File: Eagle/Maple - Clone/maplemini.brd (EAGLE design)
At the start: 32 parts, among them Q1 NPN-BJT, Q2 NPN-BJT, U1 AMS1117-3.3, X1 USB-MINIB

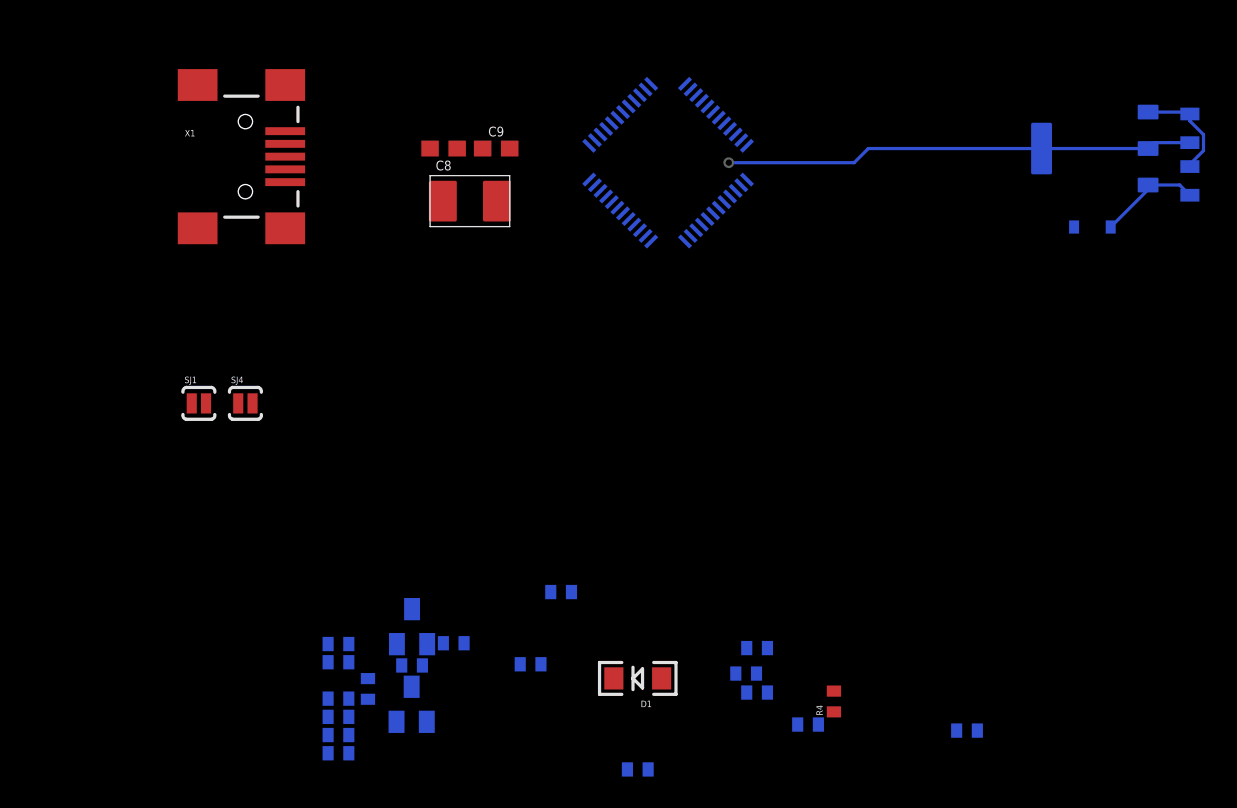
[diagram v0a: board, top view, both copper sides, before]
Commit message: reworked off proper reference boards
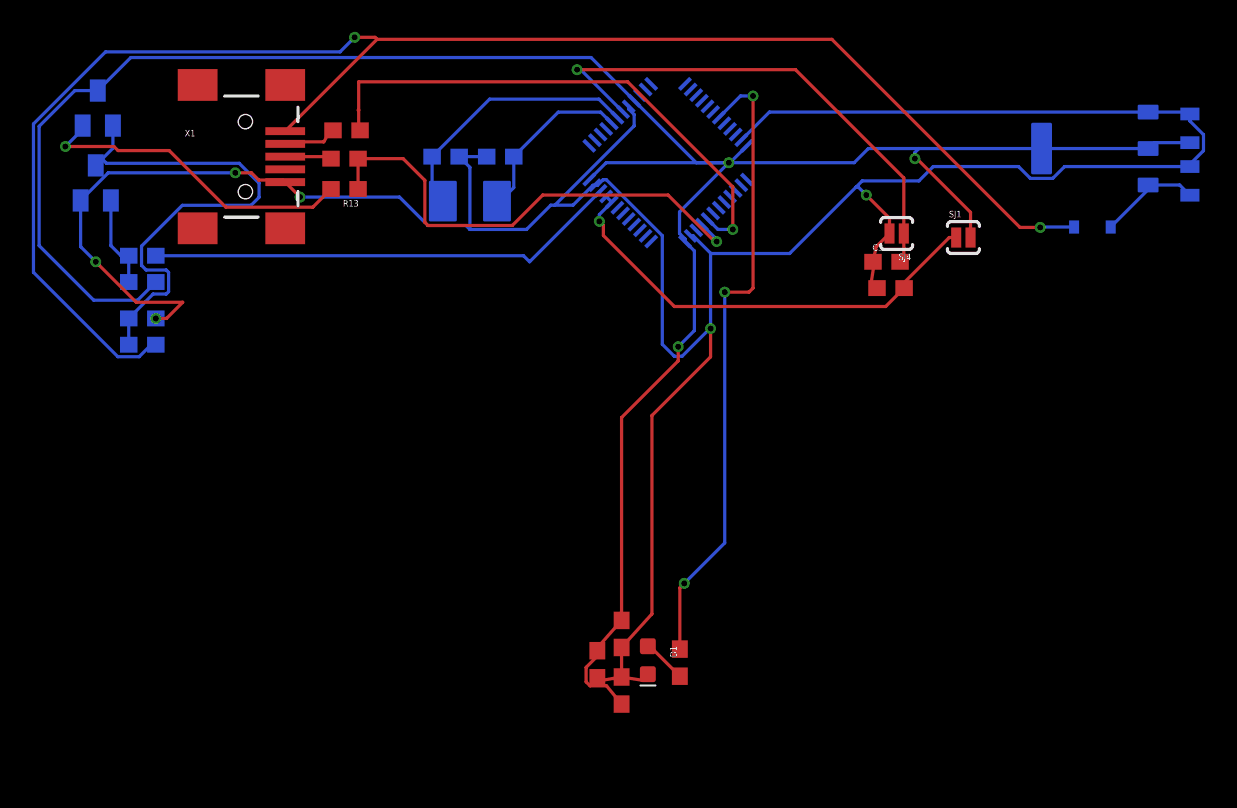
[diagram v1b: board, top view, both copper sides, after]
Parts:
- removed C10, C11: 47pF, SparkFun:C0402
- removed C4: 1uF, SparkFun:C0402
- removed Q1, Q2: NPN-BJT, SparkFun2:SOT23
- removed R10: 1.5k, SparkFun:C0402
- removed R11: 36k, SparkFun:C0402
- removed R2, R4: 1k, SparkFun:C0402
- removed R3, R8: 10k, SparkFun:C0402
- added C3: 1.0uF, SparkFun-Capacitors:0603
- added Q3, Q4: NPN-BJT, SparkFun2:SOT23
- added R13: 1.5k, SparkFun-Resistors:0603
- added R14: 1k, SparkFun-Resistors:0603
- added R15: 10k, SparkFun-Resistors:0603
- C5, C6, C7: value 1uF -> 1.0uF; device SparkFun:C0402 -> SparkFun-Capacitors:0603
- D1: device SparkFun:LED-1206 -> SparkFun-LED:LED-0603
- R1, R6, R7, R9: device SparkFun:C0402 -> SparkFun-Resistors:0603
- R12: value 47k -> 39k; device SparkFun:C0402 -> SparkFun-Resistors:0603
- R5: value 1k -> 51k; device SparkFun:C0402 -> SparkFun-Resistors:0603
- moved SJ1 49.1 mm to (45.1, 6.35)
- moved SJ4 42.3 mm to (40.9, 6.60), turned to 180 degrees
- moved R7 33.9 mm to (6.22, 11.3), flipped to the top, turned to 180 degrees
- moved R6 33.4 mm to (6.35, 13.1), flipped to the top, turned to 180 degrees
- moved R5 29.9 mm to (-6.48, 3.56), turned to 180 degrees
- moved R12 27.6 mm to (-6.48, 1.27)
- moved R9 26.7 mm to (40.5, 3.17), flipped to the top
- moved R1 8.94 mm to (27.3, -20.3), flipped to the top, turned to 90 degrees
- moved C7 8.92 mm to (23.6, -22.1), flipped to the top, turned to 90 degrees
- moved C6 7.08 mm to (22.1, -20.4), flipped to the top, turned to 270 degrees
- moved C5 6.02 mm to (23.6, -18.5), flipped to the top, turned to 270 degrees
- moved C8 3.59 mm to (16.0, 11.4), flipped to the bottom
- moved C9 3.22 mm to (12.6, 11.4), flipped to the bottom
- moved D1 1.31 mm to (25.3, -20.2), turned to 270 degrees
- flipped U$2 to the bottom
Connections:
- removed net AV+: C4.1, UC1.9
- removed net AV-: C4.2, UC1.8
- removed net N$1: R2.1, SJ1.2
- removed net N$4: R4.2, SJ4.2
- removed net N$51: Q2.2, R10.2
- removed net N$71: Q1.3, Q2.1, R11.2, R8.1
- removed net N$73: Q1.1, R12.1, R5.2
- new net N$3: Q3.2, R13.2
- new net N$6: Q4.1, R14.2, R5.1
- new net N$7: Q3.1, Q4.3, R12.2, R15.1
- net +5V/2: now also R15.2; no longer R8.2
- net 23_USBDP: now also R13.1; no longer C11.2, R10.1
- net 24_USBDM: no longer C10.2
- net DGND: now also C3.1, Q4.2, R12.1, SJ4.2, UC1.8; no longer C10.1, C11.1, Q1.2, R11.1, R4.1
- net DISC: now also R14.1; no longer R5.1
- net RESET: now also C3.2; no longer R3.1
- net VCC: now also Q3.3, R5.2, SJ1.2, UC1.9; no longer Q2.3, R12.2, R2.2, R3.2
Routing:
- net DGND: track 6.68 -> 187.6 mm, vias 0 -> 6
- net VCC: track 29.5 -> 151.9 mm, vias 1 -> 3
- net +5V/2: track 0.00 -> 100.2 mm, vias 0 -> 2
- net 33: track 0.00 -> 40.2 mm, vias 0 -> 3
- net 24_USBDM: track 0.00 -> 33.9 mm, vias 0 -> 1
- net RESET: track 0.00 -> 32.6 mm, vias 0 -> 1
- net N$7: track 0.00 -> 32.1 mm
- net 23_USBDP: track 0.00 -> 31.3 mm, vias 0 -> 1
- net DISC: track 0.00 -> 29.9 mm
- net 32: track 0.00 -> 29.0 mm, vias 0 -> 1
- net N$3: track 0.00 -> 20.6 mm, vias 0 -> 1
- net OSC_OUT: track 0.00 -> 16.5 mm
- net OSC_IN: track 0.00 -> 11.3 mm
- net N$6: track 0.00 -> 5.87 mm
- net N$60: track 0.00 -> 2.97 mm
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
